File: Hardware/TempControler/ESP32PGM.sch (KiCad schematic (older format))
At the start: 7 parts

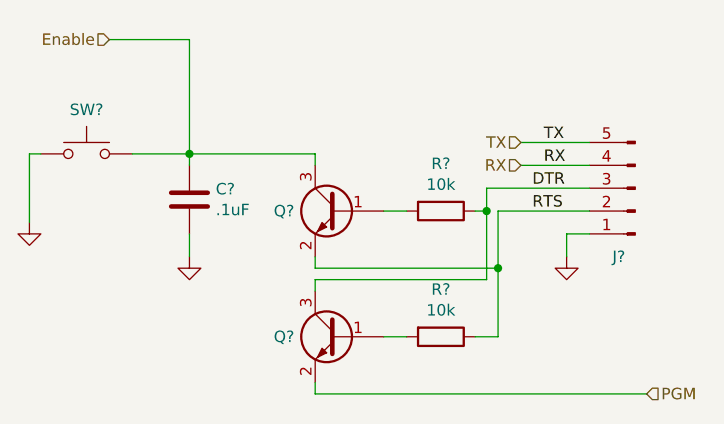
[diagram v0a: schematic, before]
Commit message: Schematic Complete
DRC - Done
Schematic - Done
Values - Done
Part Selection - In Progress
Footprint assignment- In Progress
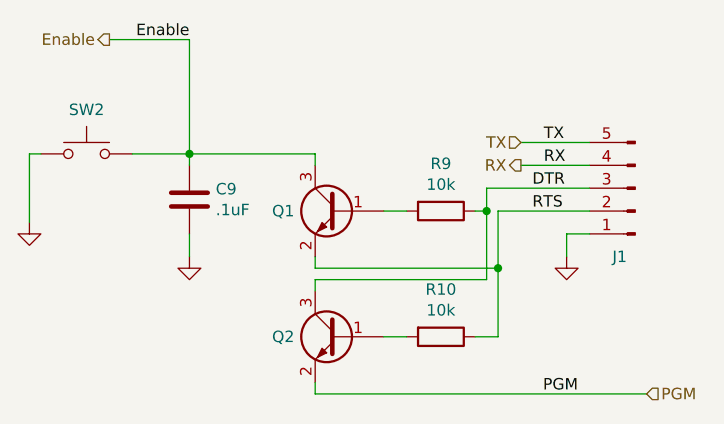
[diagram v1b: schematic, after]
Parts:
- gave numbers to parts that had none: 7
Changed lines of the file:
@@
 $Descr USLetter 11000 8500
 encoding utf-8
-Sheet 6 7
+Sheet 6 8
 Title ""
 Date ""
@@
 $EndDescr
 $Comp
-L Device:Q_NPN_BEC Q?
+L Device:Q_NPN_BEC Q1
 U 1 1 62D5678F
 P 3450 4050
-F 0 "Q?" H 3641 4050 50  0000 L CNN
+F 0 "Q1" H 3641 4050 50  0000 L CNN
 F 1 "Q_NPN_BEC" H 3641 4005 50  0001 L CNN
 F 2 "Package_TO_SOT_SMD:SOT-23" H 3650 4150 50  0001 C CNN
@@
 $EndComp
 $Comp
-L Device:Q_NPN_BEC Q?
+L Device:Q_NPN_BEC Q2
 U 1 1 62D56797
 P 3450 4600
-F 0 "Q?" H 3641 4600 50  0000 L CNN
+F 0 "Q2" H 3641 4600 50  0000 L CNN
 F 1 "Q_NPN_BEC" H 3641 4555 50  0001 L CNN
 F 2 "Package_TO_SOT_SMD:SOT-23" H 3650 4700 50  0001 C CNN
@@
 $EndComp
 $Comp
-L Device:R R?
+L Device:R R9
 U 1 1 62D5679F
 P 3900 4050
-F 0 "R?" V 3693 4050 50  0000 C CNN
+F 0 "R9" V 3693 4050 50  0000 C CNN
 F 1 "10k" V 3784 4050 50  0000 C CNN
 F 2 "Resistor_SMD:R_0603_1608Metric" V 3830 4050 50  0001 C CNN
@@
 $EndComp
 $Comp
-L Device:R R?
+L Device:R R10
 U 1 1 62D567A7
 P 3900 4600
-F 0 "R?" V 3693 4600 50  0000 C CNN
+F 0 "R10" V 3693 4600 50  0000 C CNN
 F 1 "10k" V 3784 4600 50  0000 C CNN
 F 2 "Resistor_SMD:R_0603_1608Metric" V 3830 4600 50  0001 C CNN
@@
 $EndComp
 $Comp
-L Connector:Conn_01x05_Male J?
+L Connector:Conn_01x05_Male J1
 U 1 1 62D567AF
 P 4750 3950
-F 0 "J?" H 4850 4250 50  0000 R CNN
+F 0 "J1" H 4850 4250 50  0000 R CNN
 F 1 "Conn_01x05_Male" H 4722 3973 50  0001 R CNN
 F 2 "Connector_PinSocket_2.54mm:PinSocket_1x05_P2.54mm_Vertical" H 4750 3950 50  0001 C CNN
@@
 $EndComp
 $Comp
-L Device:C C?
+L Device:C C9
 U 1 1 62D567B7
 P 2800 4000
-F 0 "C?" H 2915 4046 50  0000 L CNN
+F 0 "C9" H 2915 4046 50  0000 L CNN
 F 1 ".1uF" H 2915 3955 50  0000 L CNN
 F 2 "Capacitor_SMD:C_0805_2012Metric" H 2838 3850 50  0001 C CNN
@@
 	3350 4850 3350 4800
 $Comp
-L power:GND #PWR?
+L power:GND #PWR0123
 U 1 1 62D567D6
 P 4450 4250
-F 0 "#PWR?" H 4450 4000 50  0001 C CNN
+F 0 "#PWR0123" H 4450 4000 50  0001 C CNN
 F 1 "GND" H 4455 4077 50  0001 C CNN
 F 2 "" H 4450 4250 50  0001 C CNN
@@
 	4450 4150 4450 4250
 $Comp
-L power:GND #PWR?
+L power:GND #PWR0124
 U 1 1 62D567DE
 P 2800 4250
-F 0 "#PWR?" H 2800 4000 50  0001 C CNN
+F 0 "#PWR0124" H 2800 4000 50  0001 C CNN
 F 1 "GND" H 2805 4077 50  0001 C CNN
 F 2 "" H 2800 4250 50  0001 C CNN
@@
 $EndComp
 $Comp
-L Switch:SW_Push SW?
+L Switch:SW_Push SW2
 U 1 1 62D567E6
 P 2350 3800
-F 0 "SW?" H 2350 3993 50  0000 C CNN
+F 0 "SW2" H 2350 3993 50  0000 C CNN
 F 1 "SW_Push" H 2350 3994 50  0001 C CNN
 F 2 "misc:button SMD" H 2350 4000 50  0001 C CNN
@@
 $EndComp
 $Comp
-L power:GND #PWR?
+L power:GND #PWR0125
 U 1 1 62D567EE
 P 2100 4100
-F 0 "#PWR?" H 2100 3850 50  0001 C CNN
+F 0 "#PWR0125" H 2100 3850 50  0001 C CNN
 F 1 "GND" H 2105 3927 50  0001 C CNN
 F 2 "" H 2100 4100 50  0001 C CNN
@@
 Text HLabel 4250 3750 0    50   Input ~ 0
 TX
-Text HLabel 4250 3850 0    50   Input ~ 0
+Text HLabel 4250 3850 0    50   Output ~ 0
 RX
 Wire Wire Line
 	4250 3750 4550 3750
-Text HLabel 2450 3300 0    50   Input ~ 0
+Text HLabel 2450 3300 0    50   Output ~ 0
 Enable
 Wire Wire Line
@@
 Text HLabel 4800 4850 2    50   Input ~ 0
 PGM
+Text Label 2800 3300 2    50   ~ 0
+Enable
+Text Label 4500 4850 2    50   ~ 0
+PGM
 $EndSCHEMATC

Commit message: All Part Numbers Selected
Next step select all footprints
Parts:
- C9, J1, Q1, Q2, R10, R9, SW2: Verified True -> (none)
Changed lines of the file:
@@
 F 3 "https://www.mouser.com/datasheet/2/308/MMBT2222A-1301352.pdf" H 3450 4050 50  0001 C CNN
 F 4 "512-MMBT2222AD87Z" H 3450 4050 50  0001 C CNN "Mouser"
-F 5 "True" H 3450 4050 50  0001 C CNN "Verified"
+F 5 "" H 3450 4050 50  0001 C CNN "Verified"
 	1    3450 4050
 	-1   0    0    -1
@@
 F 3 "https://www.mouser.com/datasheet/2/308/MMBT2222A-1301352.pdf" H 3450 4600 50  0001 C CNN
 F 4 "512-MMBT2222AD87Z" H 3450 4600 50  0001 C CNN "Mouser"
-F 5 "True" H 3450 4600 50  0001 C CNN "Verified"
+F 5 "" H 3450 4600 50  0001 C CNN "Verified"
 	1    3450 4600
 	-1   0    0    -1
@@
 F 3 "https://www.mouser.com/datasheet/2/315/AOA0000C304-1149620.pdf" H 3900 4050 50  0001 C CNN
 F 4 "667-ERJ-3EKF1002V" V 3900 4050 50  0001 C CNN "Mouser"
-F 5 "True" V 3900 4050 50  0001 C CNN "Verified"
+F 5 "" V 3900 4050 50  0001 C CNN "Verified"
 	1    3900 4050
 	0    1    1    0
@@
 F 3 "https://www.mouser.com/datasheet/2/315/AOA0000C304-1149620.pdf" H 3900 4600 50  0001 C CNN
 F 4 "667-ERJ-3EKF1002V" V 3900 4600 50  0001 C CNN "Mouser"
-F 5 "True" V 3900 4600 50  0001 C CNN "Verified"
+F 5 "" V 3900 4600 50  0001 C CNN "Verified"
 	1    3900 4600
 	0    1    1    0
@@
 F 1 "Conn_01x05_Male" H 4722 3973 50  0001 R CNN
 F 2 "Connector_PinSocket_2.54mm:PinSocket_1x05_P2.54mm_Vertical" H 4750 3950 50  0001 C CNN
-F 3 "https://www.mouser.com/datasheet/2/670/pj_041h-1778780.pdf" H 4750 3950 50  0001 C CNN
+F 3 "N/A" H 4750 3950 50  0001 C CNN
 F 4 "Hand Made" H 4750 3950 50  0001 C CNN "Mouser"
-F 5 "True" H 4750 3950 50  0001 C CNN "Verified"
+F 5 "" H 4750 3950 50  0001 C CNN "Verified"
 	1    4750 3950
 	-1   0    0    1
@@
 F 3 "https://www.mouser.com/datasheet/2/212/KEM_C1002_X7R_SMD-1102033.pdf" H 2800 4000 50  0001 C CNN
 F 4 "80-C0805C104K5R" H 2800 4000 50  0001 C CNN "Mouser"
-F 5 "True" H 2800 4000 50  0001 C CNN "Verified"
+F 5 "" H 2800 4000 50  0001 C CNN "Verified"
 	1    2800 4000
 	1    0    0    -1
@@
 F 1 "SW_Push" H 2350 3994 50  0001 C CNN
 F 2 "misc:button SMD" H 2350 4000 50  0001 C CNN
-F 3 "https://www.mouser.com/datasheet/2/140/ESCHS00041_1-2544245.pdf" H 2350 4000 50  0001 C CNN
+F 3 "https://www.mouser.com/datasheet/2/140/P090002-267756.pdf" H 2350 4000 50  0001 C CNN
 F 4 "612-LL3301NF065QG" H 2350 3800 50  0001 C CNN "Mouser"
-F 5 "True" H 2350 3800 50  0001 C CNN "Verified"
+F 5 "" H 2350 3800 50  0001 C CNN "Verified"
 	1    2350 3800
 	1    0    0    -1
